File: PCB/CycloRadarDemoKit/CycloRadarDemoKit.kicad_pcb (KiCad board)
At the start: 2 copper layers, 2 parts, among them U1 ESP32-WROVER-E, U2 IP101GRI

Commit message: USB designed with TODOs, ESP part changed
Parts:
- removed U1: ESP32-WROVER-E, EspressIf:ESP32-WROVER-IE
- removed U2: IP101GRI, IP101GRI:QFN_IP101GRI_WIZ
- added D101: BAT54A, Package_TO_SOT_SMD:SOT-23, F.Cu at (162.5, 98.7)
- added D102: BAT54A, Package_TO_SOT_SMD:SOT-23, F.Cu at (162.5, 103.2)
- added D301: SP0503BAHT, Package_TO_SOT_SMD:SOT-143, F.Cu at (168.4, 90.5)
- added Q301: L8050QLT1G, Package_TO_SOT_SMD:SOT-23, F.Cu at (154.3, 99.2)
- added Q302: L8050QLT1G, Package_TO_SOT_SMD:SOT-23, F.Cu at (154.3, 103.6)
- added U101: ESP32-WROVER-E, Espressif:ESP32-WROVER-E_ThermalVias, F.Cu at (138.2, 93.2)
- added U201: IP101GRI, IP101GRI:QFN_IP101GRI_WIZ, F.Cu at (170.1, 99.8)
- added U301: CP2102N-Axx-xQFN28, Package_DFN_QFN:QFN-24-1EP_4x4mm_P0.5mm_EP2.6x2.6mm, F.Cu at (163.2, 91.4)
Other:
- board outline added: 66.6 x 44.8 mm

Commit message: PCB power manag. WIP
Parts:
- added C401: 10uF/25V(10%), Capacitor_SMD:C_1206_3216Metric, F.Cu at (125.5, 102.1)
- added C402: 10nF/50V(10%), Capacitor_SMD:C_0603_1608Metric, F.Cu at (108.8, 101.2)
- added C403: 22uF/16V(20%), Capacitor_SMD:C_1206_3216Metric, F.Cu at (125.5, 105.4)
- added R401: 0R, Resistor_SMD:R_0603_1608Metric, F.Cu at (109.4, 112.8)
- added R402: 0.2R(1%), Resistor_SMD:R_2010_5025Metric, F.Cu at (117.6, 105.4)
- added R403: 51K(1%), Resistor_SMD:R_0603_1608Metric, F.Cu at (130.4, 106.1)
- added R404: 3.6K(1%), Resistor_SMD:R_0603_1608Metric, F.Cu at (130.4, 108.6)
- added R405: R_Shunt, Resistor_SMD:R_2010_5025Metric, F.Cu at (142.3, 101.4)
- added R407: 0R, Resistor_SMD:R_0603_1608Metric, F.Cu at (125.6, 99.0)
- added U402: RT8259, Package_TO_SOT_SMD:TSOT-23-6, F.Cu at (130.9, 102.6)
- moved D101 53.1 mm to (114.9, 122.3)
- moved U201 52.7 mm to (122.5, 122.4)
- moved D102 52.7 mm to (114.9, 125.8)
- moved Q301 52.7 mm to (106.7, 121.8)
- moved Q302 52.7 mm to (106.7, 126.2)
- moved U101 52.7 mm to (90.7, 115.8)
- moved U301 52.7 mm to (115.6, 114.0)
- moved D301 46.9 mm to (128.8, 115.6)
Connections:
- U101 pad 1: Net-(U101-GND-Pad1) -> GND
- U101 pad 10: unconnected-(U101-DAC_1/ADC2_CH8/GPIO25-Pad10) -> /MAC_RXD0
- U101 pad 11: unconnected-(U101-DAC_2/ADC2_CH9/GPIO26-Pad11) -> /MAC_RXD1
- U101 pad 12: unconnected-(U101-ADC2_CH7/GPIO27-Pad12) -> /MAC_CRS_DV
- U101 pad 13: unconnected-(U101-MTMS/GPIO14/ADC2_CH6-Pad13) -> /TMS
- U101 pad 14: unconnected-(U101-MTDI/GPIO12/ADC2_CH5-Pad14) -> /TDI
- U101 pad 15: Net-(U101-GND-Pad1) -> GND
- U101 pad 16: unconnected-(U101-MTCK/GPIO13/ADC2_CH4-Pad16) -> /TCK
- U101 pad 2: unconnected-(U101-3V3-Pad2) -> +3V3
- U101 pad 23: unconnected-(U101-MTDO/GPIO15/ADC2_CH3-Pad23) -> /TDO
- U101 pad 24: unconnected-(U101-ADC2_CH2/GPIO2-Pad24) -> /GPIO2
- U101 pad 25: unconnected-(U101-GPIO0/BOOT/ADC2_CH1-Pad25) -> /MAC_CLK
- U101 pad 29: unconnected-(U101-GPIO5-Pad29) -> /PHY_RST
- U101 pad 3: unconnected-(U101-EN/CHIP_PU-Pad3) -> /EN
- U101 pad 30: unconnected-(U101-GPIO18-Pad30) -> /MAC_MDIO
- U101 pad 31: unconnected-(U101-GPIO19-Pad31) -> /MAC_TXD(0)
- U101 pad 33: unconnected-(U101-GPIO21-Pad33) -> /MAC_TX_EN
- U101 pad 34: unconnected-(U101-U0RXD/GPIO3-Pad34) -> /U0RXD
- U101 pad 35: unconnected-(U101-U0TXD/GPIO1-Pad35) -> /U0TXD
- U101 pad 36: unconnected-(U101-GPIO22-Pad36) -> /MAC_TXD(1)
- U101 pad 37: unconnected-(U101-GPIO23-Pad37) -> /MAC_MDC
- U101 pad 38: Net-(U101-GND-Pad1) -> GND
- U101 pad 39: unconnected-(U101-GND_THERMAL-Pad39) -> GND
- U201 pad 10: /IO0 -> /MAC_CLK
- U201 pad 14: /IO0 -> /MAC_CLK
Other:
- board size 66.6 x 44.8 mm -> 156.8 x 87.4 mm

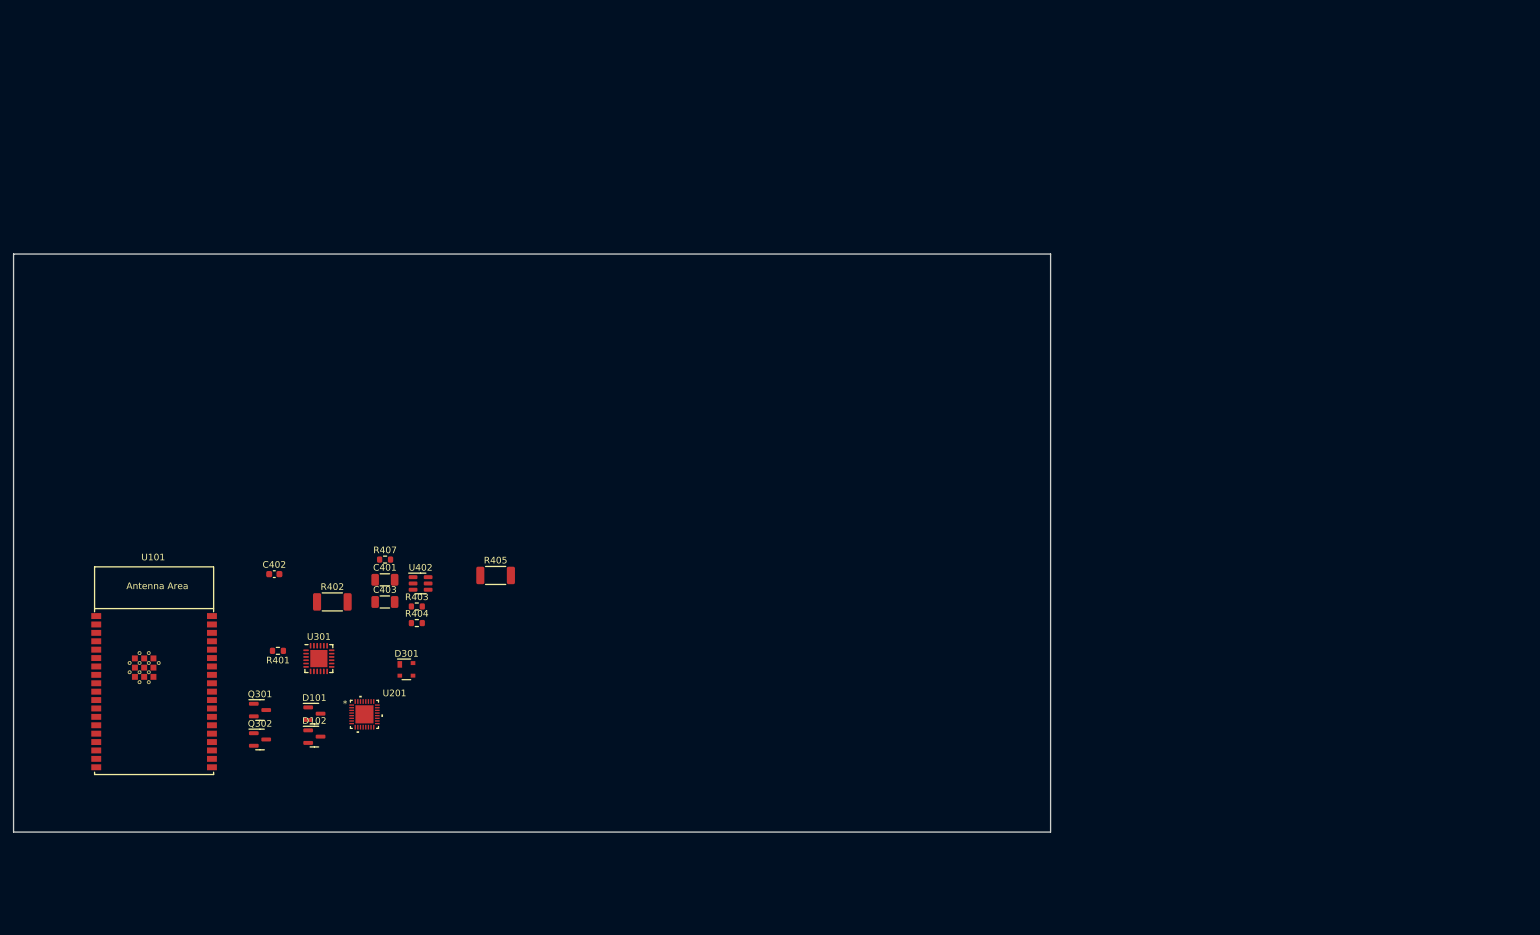
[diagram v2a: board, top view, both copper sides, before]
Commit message: Power management almost done
5V/3.3V changed to AP63203
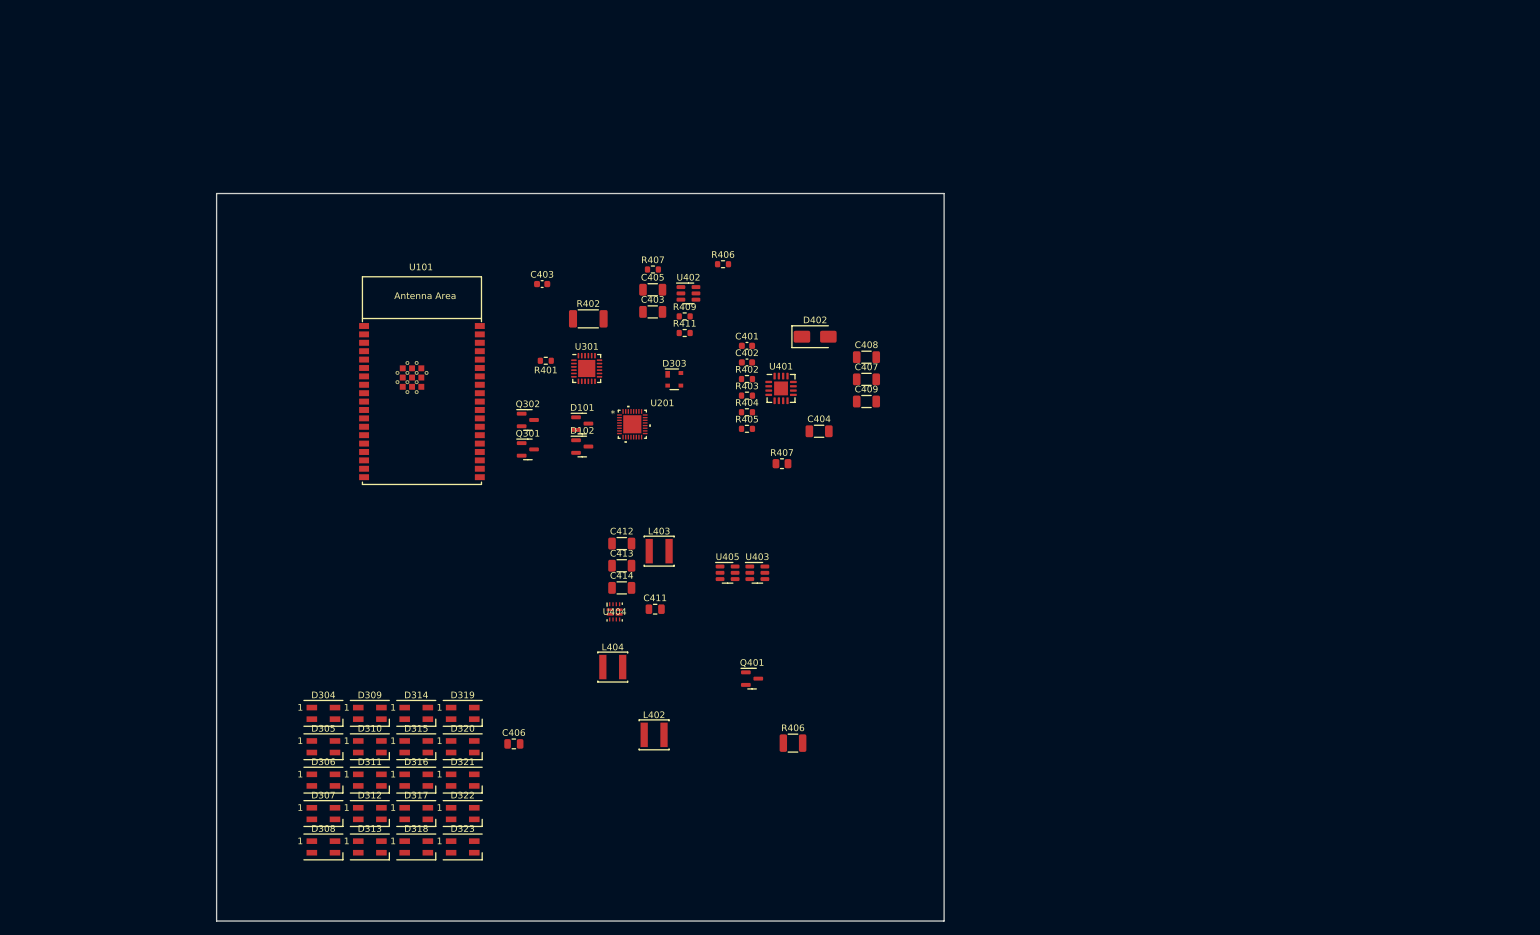
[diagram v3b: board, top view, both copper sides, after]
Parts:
- added C401: 1uF/20V(10%), Capacitor_SMD:C_0603_1608Metric, F.Cu at (180.3, 66.7)
- added C402: 1uF/20V(10%), Capacitor_SMD:C_0603_1608Metric, F.Cu at (180.3, 69.2)
- added C404: 22uF/16V(20%), Capacitor_SMD:C_1206_3216Metric, F.Cu at (191.2, 79.6)
- added C406: 100nF/50V(10%), Capacitor_SMD:C_0805_2012Metric, F.Cu at (145.0, 126.9)
- added C407: 22uF/16V(20%), Capacitor_SMD:C_1206_3216Metric, F.Cu at (198.4, 71.8)
- added C408: 10uF/25V(10%), Capacitor_SMD:C_1206_3216Metric, F.Cu at (198.4, 68.4)
- added C409: 22uF/16V(20%), Capacitor_SMD:C_1206_3216Metric, F.Cu at (198.4, 75.1)
- added C411: 100nF/50V(10%), Capacitor_SMD:C_0805_2012Metric, F.Cu at (166.4, 106.5)
- added C412: 22uF/16V(20%), Capacitor_SMD:C_1206_3216Metric, F.Cu at (161.4, 96.6)
- added C413: 10uF/25V(10%), Capacitor_SMD:C_1206_3216Metric, F.Cu at (161.4, 99.9)
- added C414: 22uF/16V(20%), Capacitor_SMD:C_1206_3216Metric, F.Cu at (161.4, 103.3)
- added D304: WS2812B, LED_SMD:LED_SK6812MINI_PLCC4_3.5x3.5mm_P1.75mm, F.Cu at (116.2, 122.2)
- added D305: WS2812B, LED_SMD:LED_SK6812MINI_PLCC4_3.5x3.5mm_P1.75mm, F.Cu at (116.2, 127.3)
- added D306: WS2812B, LED_SMD:LED_SK6812MINI_PLCC4_3.5x3.5mm_P1.75mm, F.Cu at (116.2, 132.3)
- added D307: WS2812B, LED_SMD:LED_SK6812MINI_PLCC4_3.5x3.5mm_P1.75mm, F.Cu at (116.2, 137.4)
- added D308: WS2812B, LED_SMD:LED_SK6812MINI_PLCC4_3.5x3.5mm_P1.75mm, F.Cu at (116.2, 142.4)
- added D309: WS2812B, LED_SMD:LED_SK6812MINI_PLCC4_3.5x3.5mm_P1.75mm, F.Cu at (123.3, 122.2)
- added D310: WS2812B, LED_SMD:LED_SK6812MINI_PLCC4_3.5x3.5mm_P1.75mm, F.Cu at (123.3, 127.3)
- added D311: WS2812B, LED_SMD:LED_SK6812MINI_PLCC4_3.5x3.5mm_P1.75mm, F.Cu at (123.3, 132.3)
- added D312: WS2812B, LED_SMD:LED_SK6812MINI_PLCC4_3.5x3.5mm_P1.75mm, F.Cu at (123.3, 137.4)
- added D313: WS2812B, LED_SMD:LED_SK6812MINI_PLCC4_3.5x3.5mm_P1.75mm, F.Cu at (123.3, 142.4)
- added D314: WS2812B, LED_SMD:LED_SK6812MINI_PLCC4_3.5x3.5mm_P1.75mm, F.Cu at (130.3, 122.2)
- added D315: WS2812B, LED_SMD:LED_SK6812MINI_PLCC4_3.5x3.5mm_P1.75mm, F.Cu at (130.3, 127.3)
- added D316: WS2812B, LED_SMD:LED_SK6812MINI_PLCC4_3.5x3.5mm_P1.75mm, F.Cu at (130.3, 132.3)
- added D317: WS2812B, LED_SMD:LED_SK6812MINI_PLCC4_3.5x3.5mm_P1.75mm, F.Cu at (130.3, 137.4)
- added D318: WS2812B, LED_SMD:LED_SK6812MINI_PLCC4_3.5x3.5mm_P1.75mm, F.Cu at (130.3, 142.4)
- added D319: WS2812B, LED_SMD:LED_SK6812MINI_PLCC4_3.5x3.5mm_P1.75mm, F.Cu at (137.3, 122.2)
- added D320: WS2812B, LED_SMD:LED_SK6812MINI_PLCC4_3.5x3.5mm_P1.75mm, F.Cu at (137.3, 127.3)
- added D321: WS2812B, LED_SMD:LED_SK6812MINI_PLCC4_3.5x3.5mm_P1.75mm, F.Cu at (137.3, 132.3)
- added D322: WS2812B, LED_SMD:LED_SK6812MINI_PLCC4_3.5x3.5mm_P1.75mm, F.Cu at (137.3, 137.4)
- added D323: WS2812B, LED_SMD:LED_SK6812MINI_PLCC4_3.5x3.5mm_P1.75mm, F.Cu at (137.3, 142.4)
- added D402: B230A-13-F, Diode_SMD:D_SMA, F.Cu at (190.6, 65.3)
- added L402: 4.7uH/2.85A, Inductor_SMD:L_Sunlord_SWPA4020S, F.Cu at (166.2, 125.5)
- added L403: 3.9uH/1.62A, Inductor_SMD:L_Sunlord_SWPA4020S, F.Cu at (167.0, 97.7)
- added L404: 4.7uH/2.85A, Inductor_SMD:L_Sunlord_SWPA4020S, F.Cu at (160.0, 115.2)
- added Q401: SI2309CDS, Package_TO_SOT_SMD:SOT-23, F.Cu at (181.1, 117.0)
- added R402: 10R(1%), Resistor_SMD:R_0603_1608Metric, F.Cu at (180.3, 71.7)
- added R403: 10R(1%), Resistor_SMD:R_0603_1608Metric, F.Cu at (180.3, 74.2)
- added R404: 10R(1%), Resistor_SMD:R_0603_1608Metric, F.Cu at (180.3, 76.7)
- added R405: 10R(1%), Resistor_SMD:R_0603_1608Metric, F.Cu at (180.3, 79.2)
- added R406: ???, Resistor_SMD:R_0603_1608Metric, F.Cu at (176.7, 54.3)
- added R407: 0.3R(5%), Resistor_SMD:R_0805_2012Metric, F.Cu at (185.6, 84.5)
- added U401: INA3221, Package_DFN_QFN:Texas_RGV_S-PVQFN-N16_EP2.1x2.1mm, F.Cu at (185.4, 73.1)
- added U403: AP63205WU, Package_TO_SOT_SMD:TSOT-23-6, F.Cu at (181.9, 101.0)
- added U404: TPS2121RUXR, TPS2121:TPS2121, F.Cu at (160.3, 106.9)
- added U405: AP63203WU, Package_TO_SOT_SMD:TSOT-23-6, F.Cu at (177.4, 101.0)
- R406: renamed from R405; value R_Shunt -> 0.16R(5%); footprint Resistor_SMD:R_2010_5025Metric -> Resistor_SMD:R_1210_3225Metric
- moved D101 59.7 mm to (155.4, 78.4)
- moved D102 59.7 mm to (155.4, 81.9)
- moved R409 59.7 mm to (170.9, 62.2)
- moved D303 59.7 mm to (169.3, 71.7)
- moved Q301 59.7 mm to (147.2, 82.3)
- moved Q302 59.7 mm to (147.2, 77.9)
- moved R401 59.7 mm to (149.9, 68.9)
- moved R411 59.7 mm to (170.9, 64.7)
- moved U101 59.7 mm to (131.2, 71.9)
- moved U402 59.7 mm to (171.4, 58.8)
- moved C403 59.7 mm to (149.3, 57.3)
- moved C403 59.7 mm to (166.0, 61.5)
- moved C405 59.7 mm to (166.0, 58.2)
- moved R407 59.7 mm to (166.1, 55.1)
- moved U201 59.7 mm to (163.0, 78.5)
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- renumbered C402 to C403, C401 to C405, D301 to D303, Q302 to Q301, Q301 to Q302, R403 to R409, R404 to R411
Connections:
- R406 pad 1: unconnected-(R405-Pad1) -> Net-(Q401-S)
- R406 pad 2: unconnected-(R405-Pad2) -> Net-(R403-Pad2)
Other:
- board size 156.8 x 87.4 mm -> 110 x 110 mm
- board text added: "X = 55mm Y = 55mm"

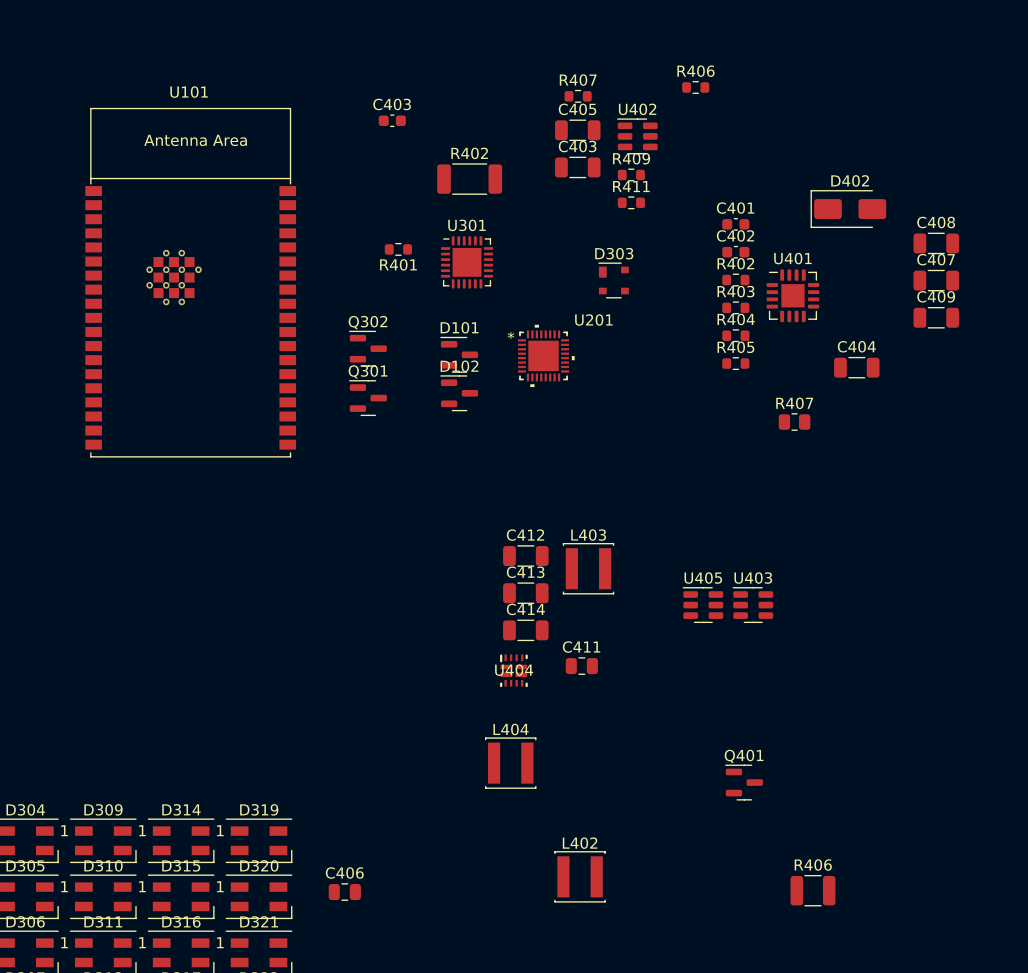
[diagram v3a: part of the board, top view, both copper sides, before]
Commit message: RJ45 chose, leds connected
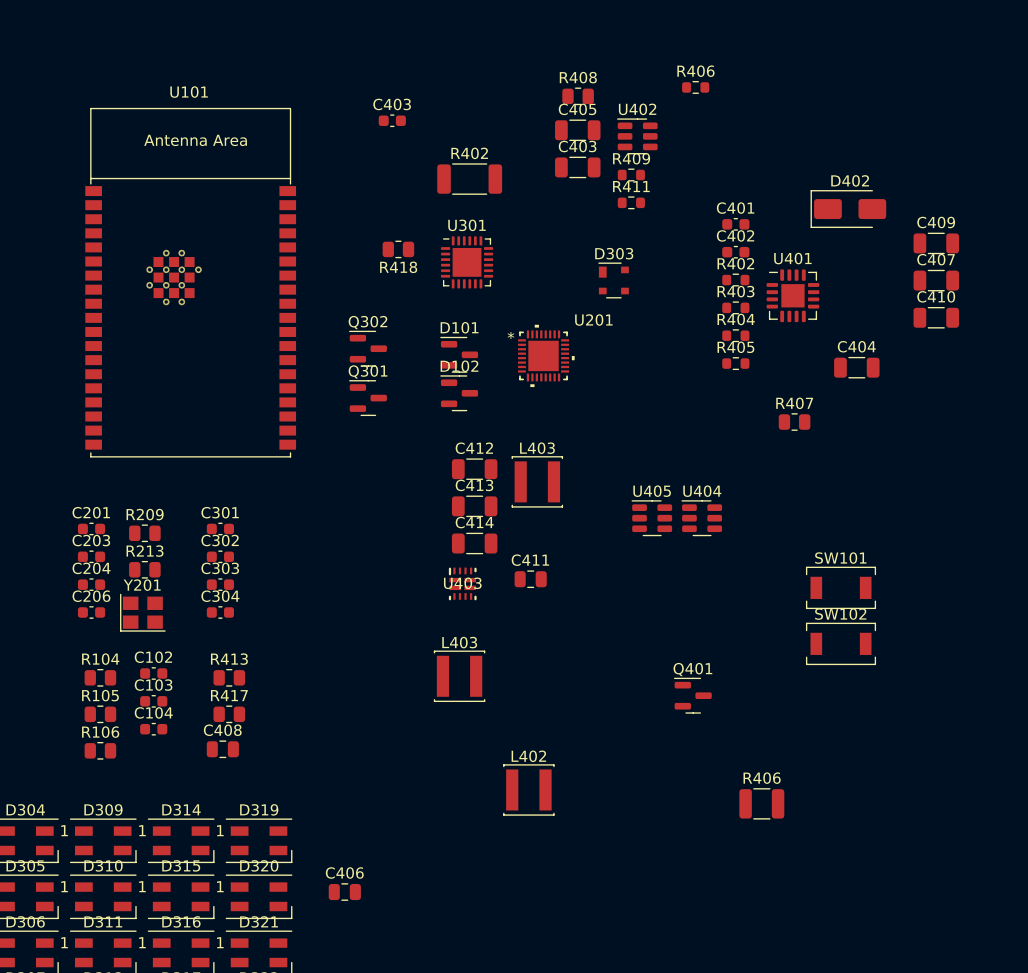
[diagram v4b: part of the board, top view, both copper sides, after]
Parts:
- added C102: 1uF/50V(10%), Capacitor_SMD:C_0603_1608Metric, F.Cu at (127.8, 107.2)
- added C103: 1uF/50V(10%), Capacitor_SMD:C_0603_1608Metric, F.Cu at (127.8, 109.7)
- added C104: 0.1uF/50V(10%), Capacitor_SMD:C_0603_1608Metric, F.Cu at (127.8, 112.2)
- added C201: 0.1uF/50V(10%), Capacitor_SMD:C_0603_1608Metric, F.Cu at (122.2, 94.1)
- added C203: 0.1uF/50V(10%), Capacitor_SMD:C_0603_1608Metric, F.Cu at (122.2, 96.7)
- added C204: 0.1uF/50V(10%), Capacitor_SMD:C_0603_1608Metric, F.Cu at (122.2, 99.2)
- added C206: 0.1uF/50V(10%), Capacitor_SMD:C_0603_1608Metric, F.Cu at (122.2, 101.7)
- added C301: 0.1uF/50V(10%), Capacitor_SMD:C_0603_1608Metric, F.Cu at (133.8, 94.1)
- added C302: 1uF/50V(10%), Capacitor_SMD:C_0603_1608Metric, F.Cu at (133.8, 96.7)
- added C303: 0.1uF/50V(10%), Capacitor_SMD:C_0603_1608Metric, F.Cu at (133.8, 99.2)
- added C304: 1uF/50V(10%), Capacitor_SMD:C_0603_1608Metric, F.Cu at (133.8, 101.7)
- added C408: 100nF/50V(10%), Capacitor_SMD:C_0805_2012Metric, F.Cu at (134.1, 114.0)
- added R104: 0R, Resistor_SMD:R_0805_2012Metric, F.Cu at (123.0, 107.6)
- added R105: 0R, Resistor_SMD:R_0805_2012Metric, F.Cu at (123.0, 110.8)
- added R106: 0R, Resistor_SMD:R_0805_2012Metric, F.Cu at (123.0, 114.1)
- added R209: 0R, Resistor_SMD:R_0805_2012Metric, F.Cu at (127.0, 94.5)
- added R213: 0R, Resistor_SMD:R_0805_2012Metric, F.Cu at (127.0, 97.8)
- added R413: 0R, Resistor_SMD:R_0805_2012Metric, F.Cu at (134.6, 107.6)
- added R417: 0R, Resistor_SMD:R_0805_2012Metric, F.Cu at (134.6, 110.8)
- added SW101: RESET, Button_Switch_SMD:SW_SPST_TS-1088R, F.Cu at (189.8, 99.5)
- added SW102: BOOT MODE, Button_Switch_SMD:SW_SPST_TS-1088R, F.Cu at (189.8, 104.5)
- added Y201: 25MHz, Crystal:Crystal_SMD_3225-4Pin_3.2x2.5mm, F.Cu at (126.8, 101.7)
- C401, C402: value 1uF/20V(10%) -> 1uF/50V(10%)
- R408: renamed from R407; footprint Resistor_SMD:R_0603_1608Metric -> Resistor_SMD:R_0805_2012Metric
- R418: renamed from R401; footprint Resistor_SMD:R_0603_1608Metric -> Resistor_SMD:R_0805_2012Metric
- moved C413 9.09 mm to (156.8, 92.1)
- moved C412 9.09 mm to (156.8, 88.8)
- moved C414 9.09 mm to (156.8, 95.5)
- moved L402 9.09 mm to (161.6, 117.7)
- moved L403 9.09 mm to (155.4, 107.4)
- moved Q401 9.09 mm to (176.4, 109.2)
- moved R406 9.09 mm to (182.6, 118.9)
- moved U404 9.09 mm to (177.2, 93.2)
- moved U405 9.09 mm to (172.8, 93.2)
- moved C411 9.09 mm to (161.8, 98.7)
- moved L403 9.09 mm to (162.4, 89.9)
- moved U403 9.09 mm to (155.7, 99.1)
- renumbered C408 to C409, C409 to C410, L404 to L403, U404 to U403, U403 to U404
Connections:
- R418 pad 1: +3V3 -> +3V3_PHY
- R418 pad 2: +3V3_PHY -> +3V3
- U101 pad 2: +3V3 -> Net-(U101-3V3)

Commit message: RJ45 footprint added
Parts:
- added J201: ARJM11B1-009-AB-EW2, Connector_RJ:RJ45_Abracon_ARJM11B1-009-AB-EW2_ABR, F.Cu at (189.3, 137.7)
- added R210: 120, Resistor_SMD:R_0603_1608Metric, F.Cu at (201.1, 127.5)
- added R212: 100, Resistor_SMD:R_0603_1608Metric, F.Cu at (201.1, 130.0)
